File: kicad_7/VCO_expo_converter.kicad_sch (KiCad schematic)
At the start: 16 parts, among them Q1 2N3904, Q2 2N3904, U1 TL072

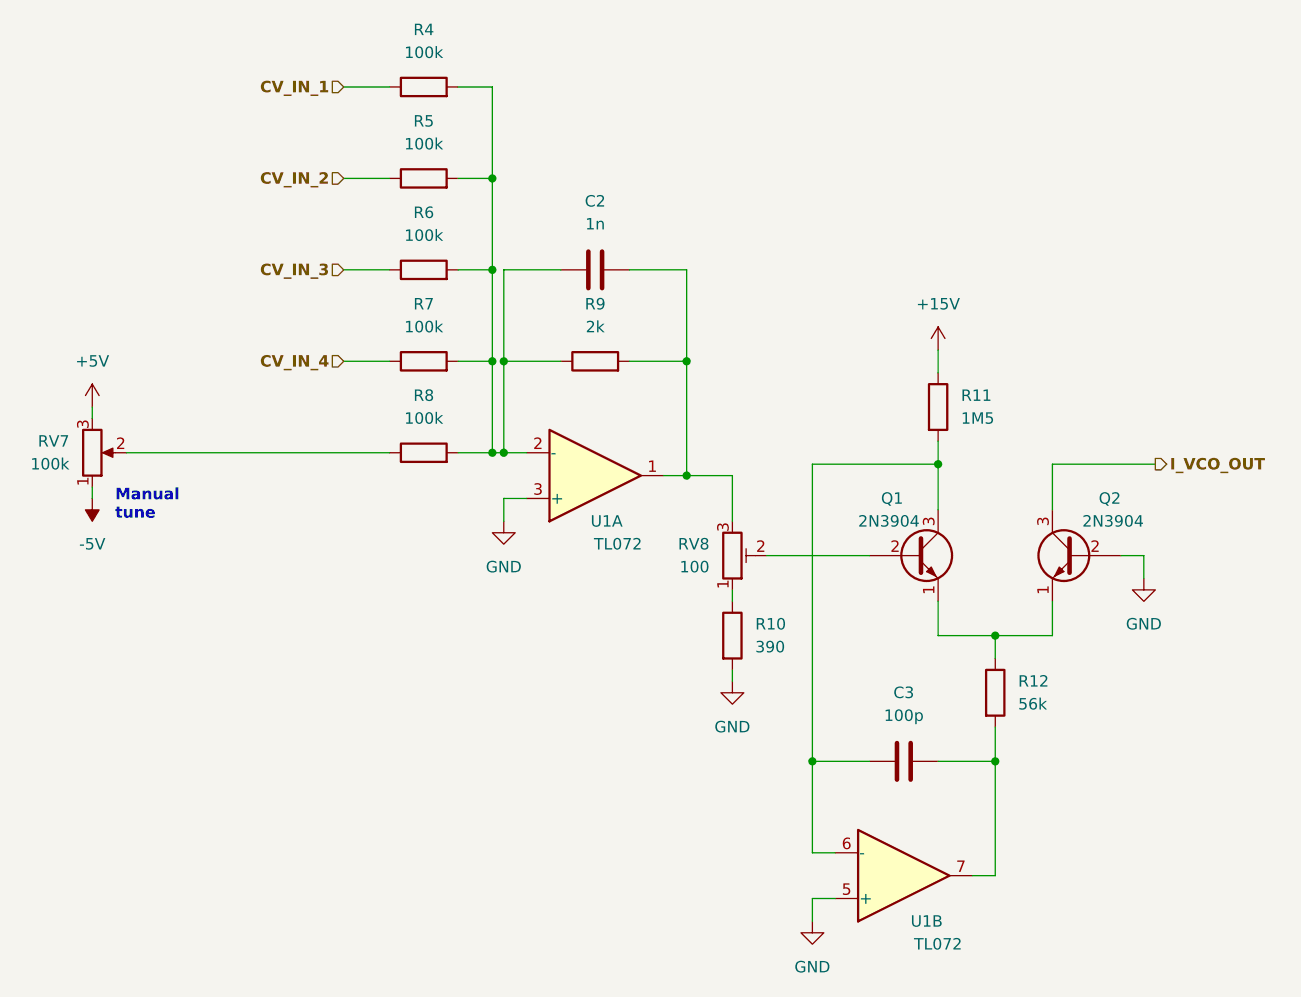
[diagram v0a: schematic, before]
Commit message: Fix external CV input circuit
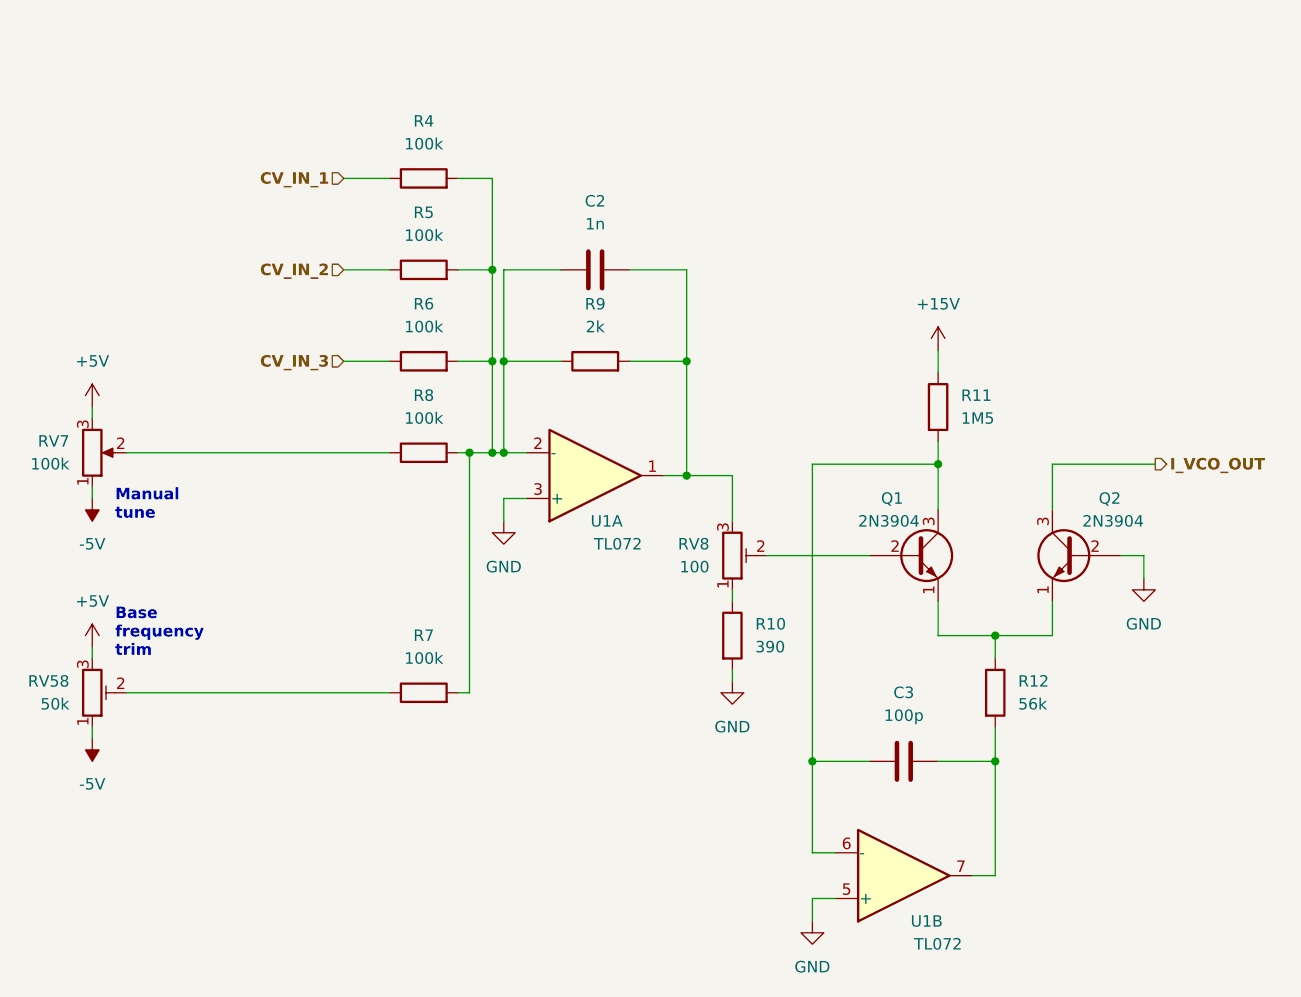
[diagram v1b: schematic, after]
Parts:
- added RV58: 50k, symbol Device:R_Potentiometer_Trim
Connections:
- net +5V: now also RV58.3
- net -5V: now also RV58.1
- net CV_IN_4: no longer names the net of R7.1
- net CV_IN_4: now also RV58.2
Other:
- note added: "Base frequency trim"
- moved on the sheet: R4, R5, R6
